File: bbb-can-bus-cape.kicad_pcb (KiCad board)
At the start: 2 copper layers, 54.6 x 86.4 mm, 2 parts, among them P8 BeagleBone_Black_Header, P9 BeagleBone_Black_Header

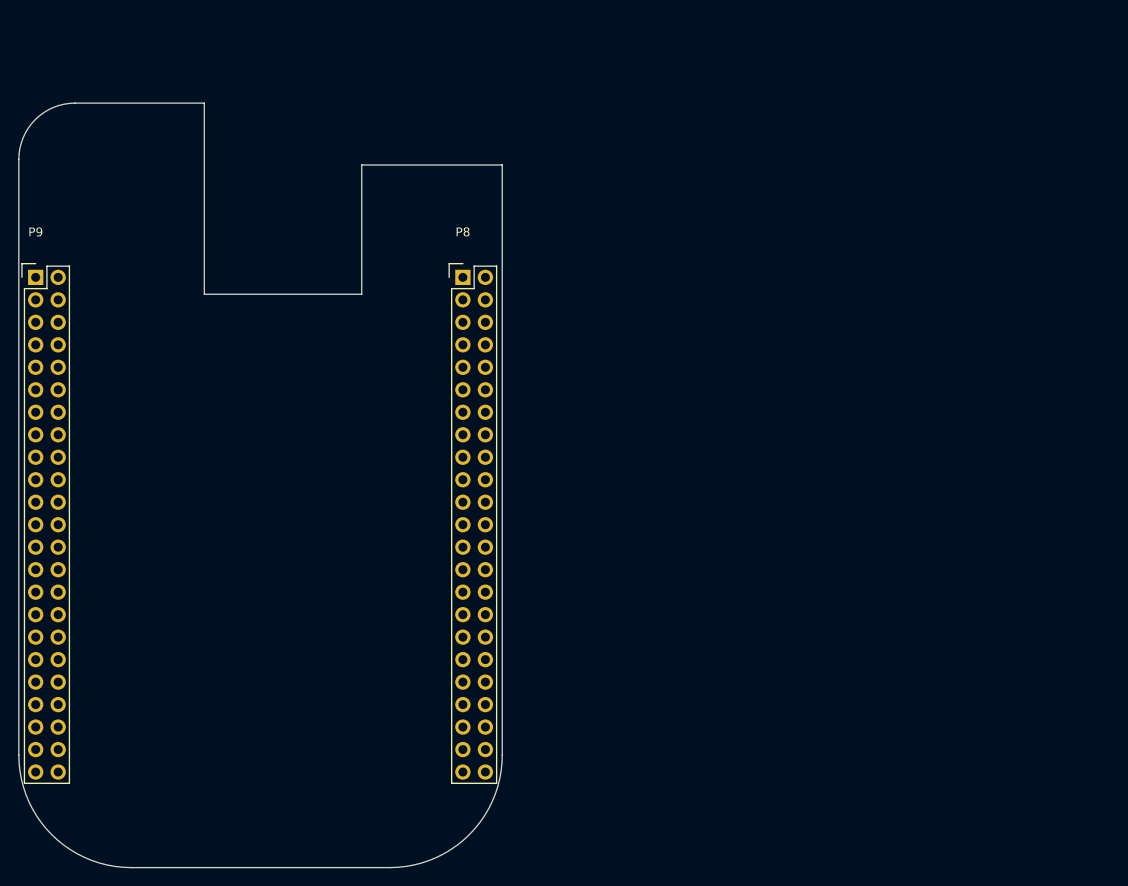
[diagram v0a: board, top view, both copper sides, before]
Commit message: Added elements and hierarchical sheets
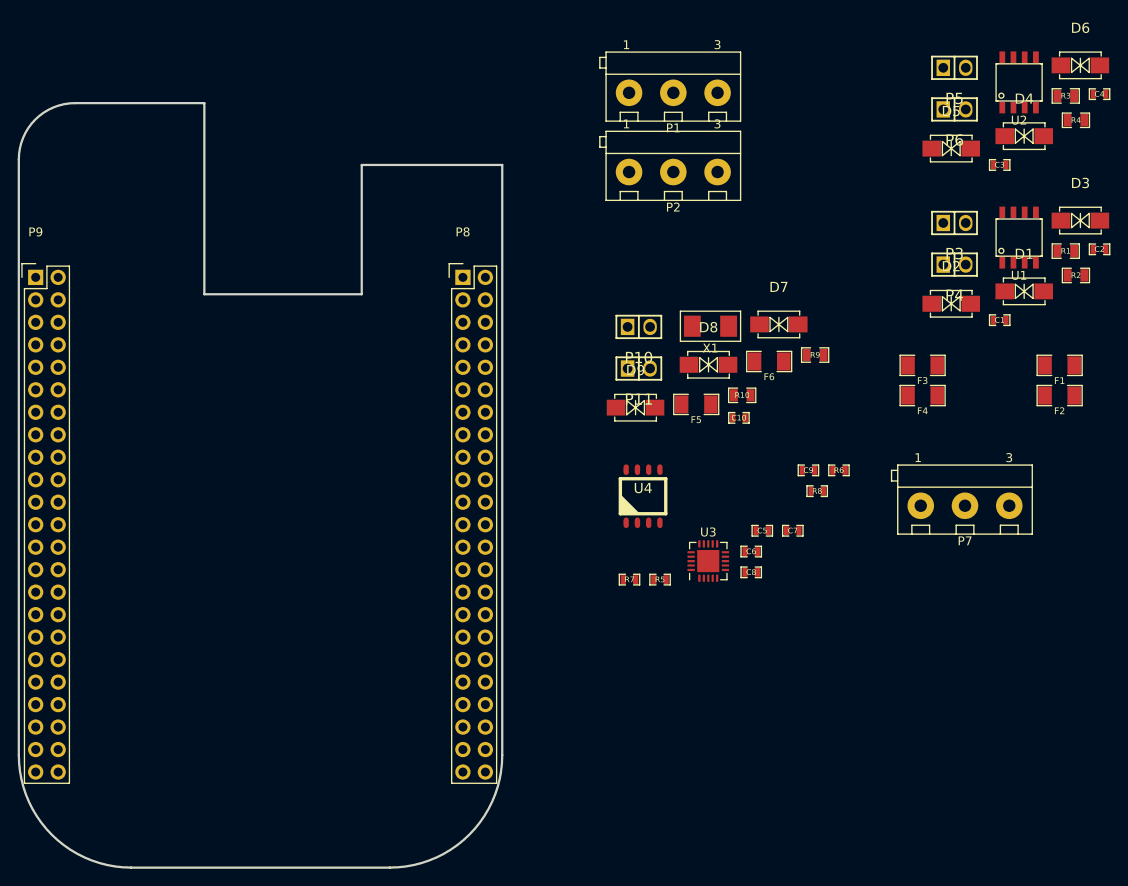
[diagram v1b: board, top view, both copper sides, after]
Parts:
- added C1: 100nF/50V, Capacitors_Smd_0603:100nF_0603, F.Cu at (225.3, 67.2)
- added C10: 100nF/50V, Capacitors_Smd_0603:100nF_0603, F.Cu at (195.8, 78.3)
- added C2: 100nF/50V, Capacitors_Smd_0603:100nF_0603, F.Cu at (236.6, 59.2)
- added C3: 100nF/50V, Capacitors_Smd_0603:100nF_0603, F.Cu at (225.3, 49.7)
- added C4: 100nF/50V, Capacitors_Smd_0603:100nF_0603, F.Cu at (236.6, 41.7)
- added C5: 100nF/50V, Capacitors_Smd_0603:100nF_0603, F.Cu at (198.5, 91.0)
- added C6: 30pF/50V, Capacitors_Smd_0603:30pF_0603, F.Cu at (197.2, 93.4)
- added C7: 30pF/50V, Capacitors_Smd_0603:30pF_0603, F.Cu at (201.9, 91.0)
- added C8: 100nF/50V, Capacitors_Smd_0603:100nF_0603, F.Cu at (197.2, 95.7)
- added C9: 100nF/50V, Capacitors_Smd_0603:100nF_0603, F.Cu at (203.7, 84.2)
- added D1: SMAJ18CA, Diodes:SMAJ18CA_SMD_DO214AC, F.Cu at (228.0, 64.0)
- added D2: SMAJ18CA, Diodes:SMAJ18CA_SMD_DO214AC, F.Cu at (219.8, 65.4)
- added D3: SMAJ18CA, Diodes:SMAJ18CA_SMD_DO214AC, F.Cu at (234.4, 56.0)
- added D4: SMAJ18CA, Diodes:SMAJ18CA_SMD_DO214AC, F.Cu at (228.0, 46.4)
- added D5: SMAJ18CA, Diodes:SMAJ18CA_SMD_DO214AC, F.Cu at (219.8, 47.8)
- added D6: SMAJ18CA, Diodes:SMAJ18CA_SMD_DO214AC, F.Cu at (234.4, 38.4)
- added D7: SMAJ18CA, Diodes:SMAJ18CA_SMD_DO214AC, F.Cu at (200.3, 67.7)
- added D8: SMAJ18CA, Diodes:SMAJ18CA_SMD_DO214AC, F.Cu at (192.4, 72.3)
- added D9: SMAJ18CA, Diodes:SMAJ18CA_SMD_DO214AC, F.Cu at (184.1, 77.1)
- added F1: SN005-60, Smd_Ptc_Fuses:SN005-60, F.Cu at (232.0, 72.3)
- added F2: SN005-60, Smd_Ptc_Fuses:SN005-60, F.Cu at (232.0, 75.7)
- added F3: SN005-60, Smd_Ptc_Fuses:SN005-60, F.Cu at (216.6, 72.3)
- added F4: SN005-60, Smd_Ptc_Fuses:SN005-60, F.Cu at (216.6, 75.7)
- added F5: SN005-60, Smd_Ptc_Fuses:SN005-60, F.Cu at (191.0, 76.7)
- added F6: SN005-60, Smd_Ptc_Fuses:SN005-60, F.Cu at (199.2, 71.9)
- added P1: DG301-5.0-03P-12-00A(H), Discrete_Connectors:DG301-5.0-03P-12-00A(H), F.Cu at (188.4, 41.5)
- added P10: TERM, Goldpin:Goldpin_2_2_54mm, F.Cu at (184.5, 68.0)
- added P11: TERM, Goldpin:Goldpin_2_2_54mm, F.Cu at (184.5, 72.7)
- added P2: DG301-5.0-03P-12-00A(H), Discrete_Connectors:DG301-5.0-03P-12-00A(H), F.Cu at (188.4, 50.5)
- added P3: TERM, Goldpin:Goldpin_2_2_54mm, F.Cu at (220.2, 56.2)
- added P4: TERM, Goldpin:Goldpin_2_2_54mm, F.Cu at (220.2, 60.9)
- added P5: TERM, Goldpin:Goldpin_2_2_54mm, F.Cu at (220.2, 38.7)
- added P6: TERM, Goldpin:Goldpin_2_2_54mm, F.Cu at (220.2, 43.4)
- added P7: DG301-5.0-03P-12-00A(H), Discrete_Connectors:DG301-5.0-03P-12-00A(H), F.Cu at (221.4, 88.2)
- added R1: 60.4R, Resistor_Smd_0805:60.4R_0805, F.Cu at (232.7, 59.4)
- added R10: 60.4R, Resistor_Smd_0805:60.4R_0805, F.Cu at (196.2, 75.7)
- added R2: 60.4R, Resistor_Smd_0805:60.4R_0805, F.Cu at (233.9, 62.2)
- added R3: 60.4R, Resistor_Smd_0805:60.4R_0805, F.Cu at (232.7, 41.9)
- added R4: 60.4R, Resistor_Smd_0805:60.4R_0805, F.Cu at (233.9, 44.6)
- added R5: 10k, Resistor_Smd_0603:10k_0603, F.Cu at (186.9, 96.5)
- added R6: 47k, Resistor_Smd_0603:47k_0603, F.Cu at (207.1, 84.2)
- added R7: 47k, Resistor_Smd_0603:47k_0603, F.Cu at (183.5, 96.5)
- added R8: 100R, Resistor_Smd_0603:100R_0603, F.Cu at (204.7, 86.5)
- added R9: 60.4R, Resistor_Smd_0805:60.4R_0805, F.Cu at (204.4, 71.2)
- added U1: IFX1050GVIOXUMA1, Communication_Interfaces:IFX1050GVIOXUMA1, F.Cu at (227.5, 57.9)
- added U2: IFX1050GVIOXUMA1, Communication_Interfaces:IFX1050GVIOXUMA1, F.Cu at (227.5, 40.4)
- added U3: MCP2515, Communication_Interfaces:MCP2515-I-QFN20, F.Cu at (192.4, 94.4)
- added U4: MCP2551, Communication_Interfaces:MCP2551_SO8, F.Cu at (185.0, 87.1)
- added X1: 8MHZ, Resonators:ABM3AIG-8.000MHZ-8-1R-T, F.Cu at (192.6, 67.9)
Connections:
- net +3V3 renamed 3V3
- net +5V renamed 5V
- net GNDD renamed GND
- P8 pad 10: Net-(P8-Pad10) -> (no net)
- P8 pad 11: Net-(P8-Pad11) -> (no net)
- P8 pad 12: Net-(P8-Pad12) -> (no net)
- P8 pad 13: Net-(P8-Pad13) -> (no net)
- P8 pad 14: Net-(P8-Pad14) -> (no net)
- P8 pad 15: Net-(P8-Pad15) -> (no net)
- P8 pad 16: Net-(P8-Pad16) -> (no net)
- P8 pad 17: Net-(P8-Pad17) -> (no net)
- P8 pad 18: Net-(P8-Pad18) -> (no net)
- P8 pad 19: Net-(P8-Pad19) -> (no net)
- P8 pad 20: Net-(P8-Pad20) -> (no net)
- P8 pad 21: Net-(P8-Pad21) -> (no net)
- P8 pad 22: Net-(P8-Pad22) -> (no net)
- P8 pad 23: Net-(P8-Pad23) -> (no net)
- P8 pad 24: Net-(P8-Pad24) -> (no net)
- P8 pad 25: Net-(P8-Pad25) -> (no net)
- P8 pad 26: Net-(P8-Pad26) -> (no net)
- P8 pad 27: Net-(P8-Pad27) -> (no net)
- P8 pad 28: Net-(P8-Pad28) -> (no net)
- P8 pad 29: Net-(P8-Pad29) -> (no net)
- P8 pad 3: Net-(P8-Pad3) -> (no net)
- P8 pad 30: Net-(P8-Pad30) -> (no net)
- P8 pad 31: Net-(P8-Pad31) -> (no net)
- P8 pad 32: Net-(P8-Pad32) -> (no net)
- P8 pad 33: Net-(P8-Pad33) -> (no net)
- P8 pad 34: Net-(P8-Pad34) -> (no net)
- P8 pad 35: Net-(P8-Pad35) -> (no net)
- P8 pad 36: Net-(P8-Pad36) -> (no net)
- P8 pad 37: Net-(P8-Pad37) -> (no net)
- P8 pad 38: Net-(P8-Pad38) -> (no net)
- P8 pad 39: Net-(P8-Pad39) -> (no net)
- P8 pad 4: Net-(P8-Pad4) -> (no net)
- P8 pad 40: Net-(P8-Pad40) -> (no net)
- P8 pad 41: Net-(P8-Pad41) -> (no net)
- P8 pad 42: Net-(P8-Pad42) -> (no net)
- P8 pad 43: Net-(P8-Pad43) -> (no net)
- P8 pad 44: Net-(P8-Pad44) -> (no net)
- P8 pad 45: Net-(P8-Pad45) -> (no net)
- P8 pad 46: Net-(P8-Pad46) -> (no net)
- P8 pad 5: Net-(P8-Pad5) -> (no net)
- P8 pad 6: Net-(P8-Pad6) -> (no net)
- P8 pad 7: Net-(P8-Pad7) -> (no net)
- P8 pad 8: Net-(P8-Pad8) -> (no net)
- P8 pad 9: Net-(P8-Pad9) -> (no net)
- P9 pad 10: SYS_RESETN -> (no net)
- P9 pad 11: Net-(P9-Pad11) -> (no net)
- P9 pad 12: Net-(P9-Pad12) -> (no net)
- P9 pad 13: Net-(P9-Pad13) -> (no net)
- P9 pad 14: Net-(P9-Pad14) -> (no net)
- P9 pad 15: Net-(P9-Pad15) -> (no net)
- P9 pad 16: Net-(P9-Pad16) -> (no net)
- P9 pad 17: Net-(P9-Pad17) -> (no net)
- P9 pad 18: Net-(P9-Pad18) -> (no net)
- P9 pad 19: Net-(P9-Pad19) -> /CAN bus0/CAN1_RD
- P9 pad 20: Net-(P9-Pad20) -> /CAN bus0/CAN1_TD
- P9 pad 21: Net-(P9-Pad21) -> (no net)
- P9 pad 22: Net-(P9-Pad22) -> (no net)
- P9 pad 23: Net-(P9-Pad23) -> (no net)
- P9 pad 24: Net-(P9-Pad24) -> /CAN bus1/CAN1_TD
- P9 pad 25: Net-(P9-Pad25) -> (no net)
- P9 pad 26: Net-(P9-Pad26) -> /CAN bus1/CAN1_RD
- P9 pad 27: Net-(P9-Pad27) -> (no net)
- P9 pad 28: Net-(P9-Pad28) -> (no net)
- P9 pad 29: Net-(P9-Pad29) -> (no net)
- P9 pad 30: Net-(P9-Pad30) -> (no net)
- P9 pad 31: Net-(P9-Pad31) -> (no net)
- P9 pad 32: VDD_ADC -> (no net)
- P9 pad 33: Net-(P9-Pad33) -> (no net)
- P9 pad 34: GNDA_ADC -> (no net)
- P9 pad 35: Net-(P9-Pad35) -> (no net)
- P9 pad 36: Net-(P9-Pad36) -> (no net)
- P9 pad 37: Net-(P9-Pad37) -> (no net)
- P9 pad 38: Net-(P9-Pad38) -> (no net)
- P9 pad 39: Net-(P9-Pad39) -> (no net)
- P9 pad 40: Net-(P9-Pad40) -> (no net)
- P9 pad 41: Net-(P9-Pad41) -> (no net)
- P9 pad 42: Net-(P9-Pad42) -> (no net)
- P9 pad 9: PWR_BUT -> (no net)
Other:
- outline, holes or cut-outs redrawn

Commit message: Schematic checked
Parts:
- added C11: 100n_50V, Capacitors_Smd_0603:100nF_0603, F.Cu at (225.7, 100.9)
- added C12: 100n_50V, Capacitors_Smd_0603:100nF_0603, F.Cu at (222.3, 103.2)
- added D10: LED_KP-2012HD, Diodes:LED_KP-2012HD_SM0805, F.Cu at (191.3, 59.1)
- added D11: LED_KP-2012SGD, Diodes:LED_KP-2012SGD_SM0805, F.Cu at (187.1, 59.1)
- added D12: LED_KP-2012YD, Diodes:LED_KP-2012YD_SM0805, F.Cu at (187.1, 61.8)
- added NTC1: NTCS0603E3103FMT, NTC_Thermistors:NTCS0603E3103FMT, F.Cu at (179.1, 81.0)
- added R11: 4k7, Resistor_Smd_0603:4k7_0603, F.Cu at (219.5, 111.2)
- added R12: 4k7, Resistor_Smd_0603:4k7_0603, F.Cu at (216.0, 111.2)
- added R13: 100R, Resistor_Smd_0603:100R_0603, F.Cu at (222.3, 100.9)
- added R14: 100R, Resistor_Smd_0603:100R_0603, F.Cu at (212.6, 110.2)
- added R15: 100R, Resistor_Smd_0603:100R_0603, F.Cu at (222.3, 105.6)
- added R16: 4k7, Resistor_Smd_0603:4k7_0603, F.Cu at (225.7, 103.2)
- added R17: 4k7, Resistor_Smd_0603:4k7_0603, F.Cu at (219.6, 108.8)
- added R18: 4k7, Resistor_Smd_0603:4k7_0603, F.Cu at (216.1, 108.8)
- added R19: 4k7, Resistor_Smd_0603:4k7_0603, F.Cu at (212.6, 112.5)
- added Sw1: DTSM-31N, Microswitches:DTSM-31N_SMD, F.Cu at (208.9, 102.0)
- added Sw2: DTSM-31N, Microswitches:DTSM-31N_SMD, F.Cu at (208.9, 106.7)
- added U5: TCN75A, Temperature_Sensors:TCN75A_SOIC8, F.Cu at (217.5, 103.7)
- added U6: DS18B20U, Temperature_Sensors:DS18B20U_MSOP-8_3x3mm_P0.65mm, F.Cu at (207.1, 111.4)
- moved R5 55.9 mm to (211.4, 46.3)
- moved C1 26.4 mm to (203.9, 51.8)
- moved C3 21.7 mm to (203.9, 46.3)
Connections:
- net /CAN bus0/CAN1_RD renamed /DCAN0_RX
- net /CAN bus0/CAN1_TD renamed /DCAN0_TX
- net /CAN bus1/CAN1_RD renamed /DCAN1_TX
- net /CAN bus1/CAN1_TD renamed /DCAN1_RX
- C1 pad 1: GND -> 5V
- C1 pad 2: 5V -> GND
- C3 pad 1: GND -> 5V
- C3 pad 2: 5V -> GND
- C5 pad 1: /Standalone Can BUS/3V3 -> 3V3
- C9 pad 1: /Standalone Can BUS/3V3 -> 3V3
- P9 pad 10: (no net) -> /SYS_RESETN
- P9 pad 15: (no net) -> Net-(P9-Pad15)
- P9 pad 17: (no net) -> /I2C1_SCL
- P9 pad 18: (no net) -> /I2C1_SDA
- P9 pad 28: (no net) -> /SPI1_CS0
- P9 pad 29: (no net) -> /SPI1_MISO
- P9 pad 30: (no net) -> /SPI1_MOSI
- P9 pad 31: (no net) -> /SPI1_SCK
- P9 pad 36: (no net) -> Net-(P9-Pad36)
- P9 pad 38: (no net) -> Net-(P9-Pad38)
- P9 pad 39: (no net) -> /AN0
- P9 pad 40: (no net) -> Net-(P9-Pad40)
- P9 pad 41: (no net) -> /GPIO0_20
- P9 pad 9: (no net) -> /PWR_BUT
- R5 pad 2: /Standalone Can BUS/3V3 -> 3V3
- R6 pad 1: /Standalone Can BUS/3V3 -> 3V3
- U3 pad 11: (no net) -> /GPIO0_20
- U3 pad 12: (no net) -> /SPI1_SCK
- U3 pad 14: (no net) -> /SPI1_MOSI
- U3 pad 15: (no net) -> /SPI1_MISO
- U3 pad 16: (no net) -> /SPI1_CS0
- U3 pad 18: /Standalone Can BUS/3V3 -> 3V3
- U3 pad 21: (no net) -> GND
- U4 pad 3: /Standalone Can BUS/3V3 -> 3V3

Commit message: Finalized project
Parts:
- removed R6, R7: 47k, Resistor_Smd_0603:47k_0603
- added C13: 100nF/50V, Capacitors_Smd_0603:100nF_0603, F.Cu at (136.0, 66.6)
- added C14: 100nF/50V, Capacitors_Smd_0603:100nF_0603, F.Cu at (135.4, 77.9)
- added C15: 30pF/50V, Capacitors_Smd_0603:30pF_0603, F.Cu at (136.2, 74.0)
- added C16: 30pF/50V, Capacitors_Smd_0603:30pF_0603, F.Cu at (127.3, 73.9)
- added C17: 100nF/50V, Capacitors_Smd_0603:100nF_0603, F.Cu at (128.3, 112.8)
- added C18: 100nF/50V, Capacitors_Smd_0603:100nF_0603, F.Cu at (138.4, 116.1)
- added D13: SMAJ7.5CA, Diodes:SMAJ7.5CA_SMD_DO214AC, F.Cu at (150.3, 67.2)
- added D14: SMAJ18CA, Diodes:SMAJ18CA_SMD_DO214AC, F.Cu at (145.1, 69.9)
- added D15: SMAJ7.5CA, Diodes:SMAJ7.5CA_SMD_DO214AC, F.Cu at (150.3, 72.5)
- added D16: SMAJ18CA, Diodes:SMAJ18CA_SMD_DO214AC, F.Cu at (137.7, 118.7)
- added D17: SMAJ18CA, Diodes:SMAJ18CA_SMD_DO214AC, F.Cu at (124.2, 118.7)
- added D18: SMAJ18CA, Diodes:SMAJ18CA_SMD_DO214AC, F.Cu at (131.0, 118.7)
- added F10: SN005-60, Smd_Ptc_Fuses:SN005-60, F.Cu at (124.0, 124.2)
- added F7: SN005-60, Smd_Ptc_Fuses:SN005-60, F.Cu at (138.9, 75.5)
- added F8: SN005-60, Smd_Ptc_Fuses:SN005-60, F.Cu at (142.1, 75.5)
- added F9: SN005-60, Smd_Ptc_Fuses:SN005-60, F.Cu at (121.1, 123.5)
- added P12: RS485, Discrete_Connectors:DG301-5.0-03P-12-00A(H), F.Cu at (125.1, 53.8)
- added P15: MCP2512-CAN, Discrete_Connectors:DG301-5.0-03P-12-00A(H), F.Cu at (133.9, 125.2)
- added R20: CRCW120610R0FKEAHP, Resistor_Smd_1206:CRCW120610R0FKEAHP, F.Cu at (140.5, 68.4)
- added R21: CRCW120610R0FKEAHP, Resistor_Smd_1206:CRCW120610R0FKEAHP, F.Cu at (140.5, 71.4)
- added R24: 100R, Resistor_Smd_0603:100R_0603, F.Cu at (138.2, 110.9)
- added R25: 60.4R, Resistor_Smd_0805:60.4R_0805, F.Cu at (140.0, 113.6)
- added R26: 60.4R, Resistor_Smd_0805:60.4R_0805, F.Cu at (138.1, 113.6)
- added R27: 100R, Resistor_Smd_0603:100R_0603, F.Cu at (137.1, 79.9)
- added R28: 4k7, Resistor_Smd_0603:4k7_0603, F.Cu at (124.4, 87.1)
- added R29: 4k7, Resistor_Smd_0603:4k7_0603, F.Cu at (122.3, 91.8)
- added R30: 100R, Resistor_Smd_0603:100R_0603, F.Cu at (122.3, 87.8)
- added R31: 100R, Resistor_Smd_0603:100R_0603, F.Cu at (122.3, 90.3)
- added REF**: KiCad-Logo_20mm_SilkScreen, Symbols:KiCad-Logo_20mm_SilkScreen, B.Cu at (130.4, 91.0)
- added Sw3: DTSM-31N, Microswitches:DTSM-31N_SMD, F.Cu at (127.2, 98.1)
- added Sw4: DTSM-31N, Microswitches:DTSM-31N_SMD, F.Cu at (122.9, 98.1)
- added U7: ISL3172EIUZ, Communication_Interfaces:ISL3172EIUZ, F.Cu at (133.6, 69.8)
- added U8: MCP2512_VDFN14, Communication_Interfaces:MCP2512_VDFN14, F.Cu at (131.8, 78.9)
- added U9: MCP2551, Communication_Interfaces:MCP2551_SO8, F.Cu at (133.0, 112.8)
- added X2: 8MHZ, Resonators:ABM3AIG-8.000MHZ-8-1R-T, F.Cu at (131.6, 74.4)
- P1: value DG301-5.0-03P-12-00A(H) -> BBB-DCAN0
- P2: value DG301-5.0-03P-12-00A(H) -> BBB-DCAN1
- P7: value DG301-5.0-03P-12-00A(H) -> MCP2515-CAN
- U3: value MCP2515 -> MCP2515_TSSOP20; footprint Communication_Interfaces:MCP2515-I-QFN20 -> Communication_Interfaces:MCP2515-I-TSSOP20
- moved D6 108.1 mm to (145.2, 99.4), turned to -90 degrees
- moved R16 108.1 mm to (122.1, 72.5), turned to 180 degrees
- moved U2 106.3 mm to (134.7, 92.3), turned to -90 degrees
- moved C4 104.1 mm to (145.9, 92.7)
- moved R4 103.1 mm to (143.6, 94.4), turned to -90 degrees
- moved R5 102.9 mm to (128.4, 107.1), turned to 180 degrees
- moved R3 101.8 mm to (143.5, 90.9), turned to -90 degrees
- moved C11 101.3 mm to (127.3, 77.0), turned to 90 degrees
- moved R12 101.0 mm to (122.1, 74.0), turned to 180 degrees
- moved R15 100.2 mm to (122.2, 110.6)
- moved R13 100.2 mm to (122.2, 105.6)
- moved R17 98.5 mm to (124.0, 85.1)
- moved R18 97.7 mm to (123.6, 77.6), turned to 180 degrees
- moved R11 97.3 mm to (122.2, 112.6)
- moved P6 96.2 mm to (140.6, 97.5), turned to 90 degrees
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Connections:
- net /Standalone Can BUS/CAN_H renamed /Standalone Can BUS/CAN_H0
- net /Standalone Can BUS/CAN_L renamed /Standalone Can BUS/CAN_L0
- net Net-(P9-Pad36) renamed /AIN5
- net Net-(P9-Pad38) renamed /AIN3
- net Net-(P9-Pad40) renamed /AIN1
- C9 pad 1: 3V3 -> 5V
- P9 pad 11: (no net) -> /UART4_RX
- P9 pad 12: (no net) -> /GPIO1_28
- P9 pad 13: (no net) -> /UART4_TX
- P9 pad 21: (no net) -> /GPIO1_17
- P9 pad 23: (no net) -> /GPIO3_21
- P9 pad 27: (no net) -> /Standalone Can BUS/CAN_~INT1~
- P9 pad 42: (no net) -> /SPI1_CS1
- U3 pad 1: (no net) -> Net-(U3-Pad1)
- U3 pad 10: (no net) -> GND
- U3 pad 11: /GPIO0_20 -> (no net)
- U3 pad 12: /SPI1_SCK -> (no net)
- U3 pad 13: (no net) -> /GPIO0_20
- U3 pad 14: /SPI1_MOSI -> /SPI1_SCK
- U3 pad 15: /SPI1_MISO -> (no net)
- U3 pad 16: /SPI1_CS0 -> /SPI1_MOSI
- U3 pad 17: Net-(C8-Pad1) -> /SPI1_MISO
- U3 pad 18: 3V3 -> /SPI1_CS0
- U3 pad 19: Net-(U3-Pad19) -> Net-(C8-Pad1)
- U3 pad 2: (no net) -> Net-(U3-Pad2)
- U3 pad 20: Net-(U3-Pad20) -> 3V3
- U3 pad 6: Net-(C6-Pad1) -> (no net)
- U3 pad 7: Net-(C7-Pad1) -> (no net)
- U3 pad 8: GND -> Net-(C6-Pad1)
- U3 pad 9: (no net) -> Net-(C7-Pad1)
- U4 pad 1: Net-(U3-Pad19) -> Net-(U3-Pad1)
- U4 pad 3: 3V3 -> 5V
- U4 pad 4: Net-(U3-Pad20) -> Net-(U3-Pad2)
- U4 pad 5: Net-(R6-Pad2) -> 3V3
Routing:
- net 3V3: track 0.00 -> 165.8 mm, vias 0 -> 11
- net 5V: track 0.00 -> 86.5 mm, vias 0 -> 6
- net Net-(U8-Pad2): track 0.00 -> 53.9 mm, vias 0 -> 2
- net /SPI1_SCK: track 0.00 -> 51.6 mm, vias 0 -> 2
- net GND: track 0.00 -> 48.5 mm, vias 0 -> 69
- net /SPI1_CS1: track 0.00 -> 46.7 mm, vias 0 -> 3
- net /SPI1_MOSI: track 0.00 -> 45.3 mm, vias 0 -> 2
- net Net-(U8-Pad1): track 0.00 -> 44.9 mm, vias 0 -> 2
- net /SPI1_MISO: track 0.00 -> 40.1 mm, vias 0 -> 2
- net Net-(D16-Pad2): track 0.00 -> 38.1 mm
- net Net-(D7-Pad2): track 0.00 -> 33.5 mm, vias 0 -> 2
- net /GPIO0_20: track 0.00 -> 32.8 mm
- net /CAN bus0/CAN_L: track 0.00 -> 32.1 mm
- net /Standalone Can BUS/CAN_~INT1~: track 0.00 -> 31.9 mm, vias 0 -> 3
- net /RS485/RS485_A: track 0.00 -> 31.2 mm, vias 0 -> 1
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- added copper zone on B.Cu, net GND
- added copper zone on F.Cu, net GND
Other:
- board text added: "A"
- board text added: "B"
- board text added: "DCAN0"
- board text added: "DCAN1"
- board text added: "GND"
- board text added: "H"
- board text added: "INTERFACE BOARD V1.0"
- board text added: "L"
- board text added: "MCP2512-CAN"
- board text added: "MCP2515-CAN"
- board text added: "RS485"

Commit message: Finalized project
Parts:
- removed D13, D15: SMAJ7.5CA, Diodes:SMAJ7.5CA_SMD_DO214AC
- removed D14, D16, D17, D18, D6, D7, D8, D9: SMAJ18CA, Diodes:SMAJ18CA_SMD_DO214AC
- D1, D2, D3, D4: value SMAJ18CA -> PESD2CAN; footprint Diodes:SMAJ18CA_SMD_DO214AC -> ESD_Protectors:PESD2CAN.215
- D5: value SMAJ18CA -> SM712.TCT; footprint Diodes:SMAJ18CA_SMD_DO214AC -> ESD_Protectors:SM712.TCT
- moved D4 31.7 mm to (136.3, 118.8), turned to 90 degrees
- moved D3 26.3 mm to (156.2, 115.5), turned to 180 degrees
- moved D5 24.2 mm to (146.0, 70.0)
- moved D2 11.5 mm to (149.4, 94.3)
- moved D1 6.81 mm to (152.1, 83.1), turned to -90 degrees
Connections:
- D1 pad 1: GND -> Net-(D1-Pad1)
- D2 pad 1: Net-(D1-Pad2) -> Net-(D2-Pad1)
- D3 pad 1: Net-(D2-Pad2) -> Net-(D3-Pad1)
- D3 pad 2: GND -> Net-(D3-Pad2)
- D4 pad 1: GND -> Net-(D4-Pad1)
- D5 pad 1: Net-(D4-Pad2) -> Net-(D5-Pad1)
- F10 pad 1: Net-(D17-Pad2) -> Net-(D4-Pad1)
- F2 pad 1: Net-(D2-Pad2) -> Net-(D1-Pad1)
- F3 pad 1: Net-(D4-Pad2) -> Net-(D2-Pad2)
- F4 pad 1: Net-(D5-Pad2) -> Net-(D2-Pad1)
- F5 pad 1: Net-(D7-Pad2) -> Net-(D3-Pad2)
- F6 pad 1: Net-(D8-Pad2) -> Net-(D3-Pad1)
- F7 pad 1: Net-(D13-Pad2) -> Net-(D5-Pad2)
- F8 pad 1: Net-(D14-Pad2) -> Net-(D5-Pad1)
- F9 pad 1: Net-(D16-Pad2) -> Net-(D4-Pad2)
- P10 pad 2: Net-(D7-Pad2) -> Net-(D3-Pad2)
- P11 pad 1: Net-(D8-Pad2) -> Net-(D3-Pad1)
- P4 pad 1: Net-(D2-Pad2) -> Net-(D1-Pad1)
- P5 pad 2: Net-(D4-Pad2) -> Net-(D2-Pad2)
- P6 pad 1: Net-(D5-Pad2) -> Net-(D2-Pad1)
- P9 pad 21: /GPIO1_17 -> /GPIO0_3
- P9 pad 22: (no net) -> /GPIO0_2
- P9 pad 23: /GPIO3_21 -> /GPIO1_17
- P9 pad 25: (no net) -> /GPIO3_21
- P9 pad 36: /AIN5 -> (no net)
- P9 pad 37: (no net) -> Net-(P9-Pad37)
- P9 pad 38: /AIN3 -> (no net)
- P9 pad 40: /AIN1 -> (no net)
- R13 pad 1: /AIN5 -> /GPIO1_17
- R14 pad 1: /AIN3 -> /GPIO0_2
- R15 pad 1: /AIN1 -> /GPIO3_21
- R20 pad 1: Net-(D13-Pad2) -> Net-(D5-Pad2)
- R21 pad 1: Net-(D14-Pad2) -> Net-(D5-Pad1)
- R25 pad 1: Net-(D16-Pad2) -> Net-(D4-Pad2)
- R26 pad 2: Net-(D17-Pad2) -> Net-(D4-Pad1)
- R30 pad 2: /GPIO1_17 -> /GPIO0_3
- R31 pad 2: /GPIO3_21 -> Net-(P9-Pad37)
- U1 pad 6: Net-(D2-Pad2) -> Net-(D1-Pad1)
- U2 pad 6: Net-(D5-Pad2) -> Net-(D2-Pad1)
- U2 pad 7: Net-(D4-Pad2) -> Net-(D2-Pad2)
- U4 pad 6: Net-(D8-Pad2) -> Net-(D3-Pad1)
- U4 pad 7: Net-(D7-Pad2) -> Net-(D3-Pad2)
- U9 pad 6: Net-(D17-Pad2) -> Net-(D4-Pad1)
- U9 pad 7: Net-(D16-Pad2) -> Net-(D4-Pad2)
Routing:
- net Net-(D16-Pad2): track 38.1 -> 0.00 mm
- net Net-(D7-Pad2): track 33.5 -> 0.00 mm, vias 2 -> 0
- net Net-(D3-Pad2): track 0.00 -> 31.0 mm, vias 0 -> 2
- net Net-(P9-Pad37): track 0.00 -> 28.6 mm, vias 0 -> 2
- net Net-(D3-Pad1): track 0.00 -> 25.7 mm
- net Net-(D8-Pad2): track 25.5 -> 0.00 mm
- net /GPIO0_2: track 0.00 -> 22.7 mm, vias 0 -> 2
- net Net-(D4-Pad1): track 0.00 -> 22.0 mm
- net Net-(D2-Pad1): track 0.00 -> 22.0 mm
- net Net-(D17-Pad2): track 19.0 -> 0.00 mm
- net /GPIO3_21: track 6.28 -> 21.1 mm, vias 0 -> 2
- net /GPIO1_17: track 6.18 -> 20.8 mm, vias 0 -> 2
- net Net-(D1-Pad1): track 0.00 -> 14.4 mm, vias 0 -> 1
- net Net-(D13-Pad2): track 13.3 -> 0.00 mm
- net Net-(D4-Pad2): track 23.5 -> 34.8 mm
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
